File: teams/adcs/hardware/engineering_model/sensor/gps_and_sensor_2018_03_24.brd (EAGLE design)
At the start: 94 x 94 mm, 50 parts, among them U1 LT1761-X, U2 LT1761-X, U3 OEM719, U4 LTC3624

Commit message: ADCS/Sensor: Use picolock with more connectors and reformat component values
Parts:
- C1, C18, C2, C20, C22, C9: value 1u -> 1uF
- C10: value 22p -> 22pF
- C11, C17, C19, C21: value 10u -> 10uF
- C12: value 47u -> 47uF
- C13: value 22u -> 22uF
- C14, C15: value 230u -> DNP
- C16: value 1 uF -> 1uF
- C3, C4: value 4.7u -> 4.7uF
- C5, C6: value 0.01u -> 0.01uF
- C7: value 2.2u -> 2.2uF
- C8, C_SLEW_1: value 0.1u -> 0.1uF
- R5: value (none) -> 330
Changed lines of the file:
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@@
 <element name="U3" library="DubSat1 Components" package="OEM719" value="OEM719" x="62.484" y="5.842" rot="R90"/>
 <element name="U1" library="DubSat1 Components" package="SOT-23-5" value="LT1761-X" x="86.995" y="80.9625" rot="R270"/>
-<element name="C5" library="DubSat1 Components" package="0805" value="0.01u" x="90.17" y="80.9625" rot="R270"/>
-<element name="C1" library="DubSat1 Components" package="0805" value="1u" x="85.4075" y="84.455" rot="R270"/>
-<element name="C3" library="DubSat1 Components" package="0805" value="4.7u" x="92.3925" y="80.9625" rot="R90"/>
+<element name="C5" library="DubSat1 Components" package="0805" value="0.01uF" x="90.17" y="80.9625" rot="R270"/>
+<element name="C1" library="DubSat1 Components" package="0805" value="1uF" x="85.4075" y="84.455" rot="R270"/>
+<element name="C3" library="DubSat1 Components" package="0805" value="4.7uF" x="92.3925" y="80.9625" rot="R90"/>
 <element name="U2" library="DubSat1 Components" package="SOT-23-5" value="LT1761-X" x="14.605" y="80.9625" rot="R90"/>
-<element name="C6" library="DubSat1 Components" package="0805" value="0.01u" x="11.1125" y="80.9625" rot="R90"/>
-<element name="C2" library="DubSat1 Components" package="0805" value="1u" x="16.1925" y="84.455" rot="R270"/>
-<element name="C4" library="DubSat1 Components" package="0805" value="4.7u" x="8.89" y="80.9625" rot="R270"/>
+<element name="C6" library="DubSat1 Components" package="0805" value="0.01uF" x="11.1125" y="80.9625" rot="R90"/>
+<element name="C2" library="DubSat1 Components" package="0805" value="1uF" x="16.1925" y="84.455" rot="R270"/>
+<element name="C4" library="DubSat1 Components" package="0805" value="4.7uF" x="8.89" y="80.9625" rot="R270"/>
 <element name="PHOTODIODE" library="DubSat1 Components" package="PICOLOCK_4" value="PICOLOCK_4" x="76.708" y="14.986" rot="R180"/>
 <element name="R1" library="DubSat1 Components" package="0805" value="2.2k" x="67.31" y="12.954" rot="R270"/>
 <element name="R2" library="DubSat1 Components" package="0805" value="2.2k" x="67.31" y="8.89" rot="R270"/>
 <element name="U4" library="DubSat1 Components" package="LTC3624" value="LTC3624" x="69.596" y="70.612" rot="R270"/>
-<element name="C7" library="DubSat1 Components" package="0805" value="2.2u" x="70.358" y="66.294" rot="R270"/>
+<element name="C7" library="DubSat1 Components" package="0805" value="2.2uF" x="70.358" y="66.294" rot="R270"/>
 <element name="L1" library="DubSat1 Components" package="COILCRAFT_XAL4020" value="COILCRAFT_XAL4020-222ME" x="71.882" y="74.93"/>
 <element name="R3" library="DubSat1 Components" package="0805" value="0" x="72.898" y="67.818" rot="R90"/>
 <element name="R4" library="DubSat1 Components" package="0805" value="DNP" x="68.072" y="66.294" rot="R90"/>
-<element name="C10" library="DubSat1 Components" package="0805" value="22p" x="73.914" y="64.516"/>
-<element name="C8" library="DubSat1 Components" package="0805" value="0.1u" x="76.2" y="69.977"/>
-<element name="C9" library="DubSat1 Components" package="0805" value="1u" x="76.2" y="71.755"/>
-<element name="C11" library="DubSat1 Components" package="0805" value="10u" x="76.2" y="68.199"/>
-<element name="C12" library="DubSat1 Components" package="1206" value="47u" x="76.581" y="75.819"/>
+<element name="C10" library="DubSat1 Components" package="0805" value="22pF" x="73.914" y="64.516"/>
+<element name="C8" library="DubSat1 Components" package="0805" value="0.1uF" x="76.2" y="69.977"/>
+<element name="C9" library="DubSat1 Components" package="0805" value="1uF" x="76.2" y="71.755"/>
+<element name="C11" library="DubSat1 Components" package="0805" value="10uF" x="76.2" y="68.199"/>
+<element name="C12" library="DubSat1 Components" package="1206" value="47uF" x="76.581" y="75.819"/>
 <element name="U$1" library="HuskySat-1 Logos" package="LOGO_MOLEX" value="LOGO_MOLEX" x="37.846" y="13.462" rot="MR0"/>
-<element name="C_SLEW_1" library="DubSat1 Components" package="0805" value="0.1u" x="71.12" y="55.88"/>
+<element name="C_SLEW_1" library="DubSat1 Components" package="0805" value="0.1uF" x="71.12" y="55.88"/>
 <element name="R_PULLUP1" library="DubSat1 Components" package="0805" value="100k" x="73.66" y="58.42" smashed="yes" rot="R270">
 <attribute name="NAME" x="74.617325" y="59.63869375" size="0.4064" layer="25" font="vector" rot="R270"/>
@@
 </element>
 <element name="U$3" library="DubSat1 Components" package="TSOP-6" value="SI3865DDV" x="71.12" y="58.42" rot="R270"/>
-<element name="C14" library="DubSat1 Components" package="PANASONIC_SVPG" value="230u" x="87.63" y="57.912" rot="R270"/>
-<element name="C15" library="DubSat1 Components" package="PANASONIC_SVPG" value="230u" x="81.28" y="61.976" rot="R90"/>
-<element name="C13" library="DubSat1 Components" package="1206" value="22u" x="76.581" y="73.66"/>
+<element name="C14" library="DubSat1 Components" package="PANASONIC_SVPG" value="DNP" x="87.63" y="57.912" rot="R270"/>
+<element name="C15" library="DubSat1 Components" package="PANASONIC_SVPG" value="DNP" x="81.28" y="61.976" rot="R90"/>
+<element name="C13" library="DubSat1 Components" package="1206" value="22uF" x="76.581" y="73.66"/>
 <element name="U$2" library="DubSat1 Components" package="1X08_CONNECTOR" value="PROGRAM/DEBUG_PORT" x="93.218" y="15.748" rot="R90"/>
 <element name="D1" library="DubSat1 Components" package="LED-1206" value="" x="88.392" y="36.83" rot="R90"/>
-<element name="R5" library="DubSat1 Components" package="0805" value="" x="90.424" y="37.846" rot="R90"/>
+<element name="R5" library="DubSat1 Components" package="0805" value="330" x="90.424" y="37.846" rot="R90"/>
 <element name="J1" library="SparkFun-Connectors" package="1X06_LOCK" value="" x="64.516" y="63.754" rot="R90"/>
 <element name="J2" library="SparkFun-Connectors" package="1X03_LOCK" value="" x="64.262" y="12.446" rot="R270"/>
@@
 <attribute name="PROD_ID" value="CONN-09701" x="84.582" y="7.874" size="1.778" layer="27" rot="R90" display="off"/>
 </element>
-<element name="C16" library="DubSat1 Components" package="0805" value="1 uF" x="75.946" y="50.038"/>
-<element name="C17" library="DubSat1 Components" package="0805" value="10u" x="67.691" y="74.295" rot="R180"/>
-<element name="C18" library="DubSat1 Components" package="0805" value="1u" x="69.85" y="77.978"/>
-<element name="C19" library="DubSat1 Components" package="0805" value="10u" x="73.66" y="55.118" rot="R270"/>
-<element name="C20" library="DubSat1 Components" package="0805" value="1u" x="75.438" y="55.118" rot="R270"/>
-<element name="C21" library="DubSat1 Components" package="0805" value="10u" x="67.564" y="60.452" rot="R90"/>
-<element name="C22" library="DubSat1 Components" package="0805" value="1u" x="71.12" y="53.34" rot="R315"/>
+<element name="C16" library="DubSat1 Components" package="0805" value="1uF" x="75.946" y="50.038"/>
+<element name="C17" library="DubSat1 Components" package="0805" value="10uF" x="67.691" y="74.295" rot="R180"/>
+<element name="C18" library="DubSat1 Components" package="0805" value="1uF" x="69.85" y="77.978"/>
+<element name="C19" library="DubSat1 Components" package="0805" value="10uF" x="73.66" y="55.118" rot="R270"/>
+<element name="C20" library="DubSat1 Components" package="0805" value="1uF" x="75.438" y="55.118" rot="R270"/>
+<element name="C21" library="DubSat1 Components" package="0805" value="10uF" x="67.564" y="60.452" rot="R90"/>
+<element name="C22" library="DubSat1 Components" package="0805" value="1uF" x="71.12" y="53.34" rot="R315"/>
 <element name="R_PULLDOWN" library="DubSat1 Components" package="0805" value="100k" x="78.486" y="54.356" rot="R90"/>
 <element name="R6" library="DubSat1 Components" package="0805" value="100k" x="61.214" y="23.622" rot="R90"/>

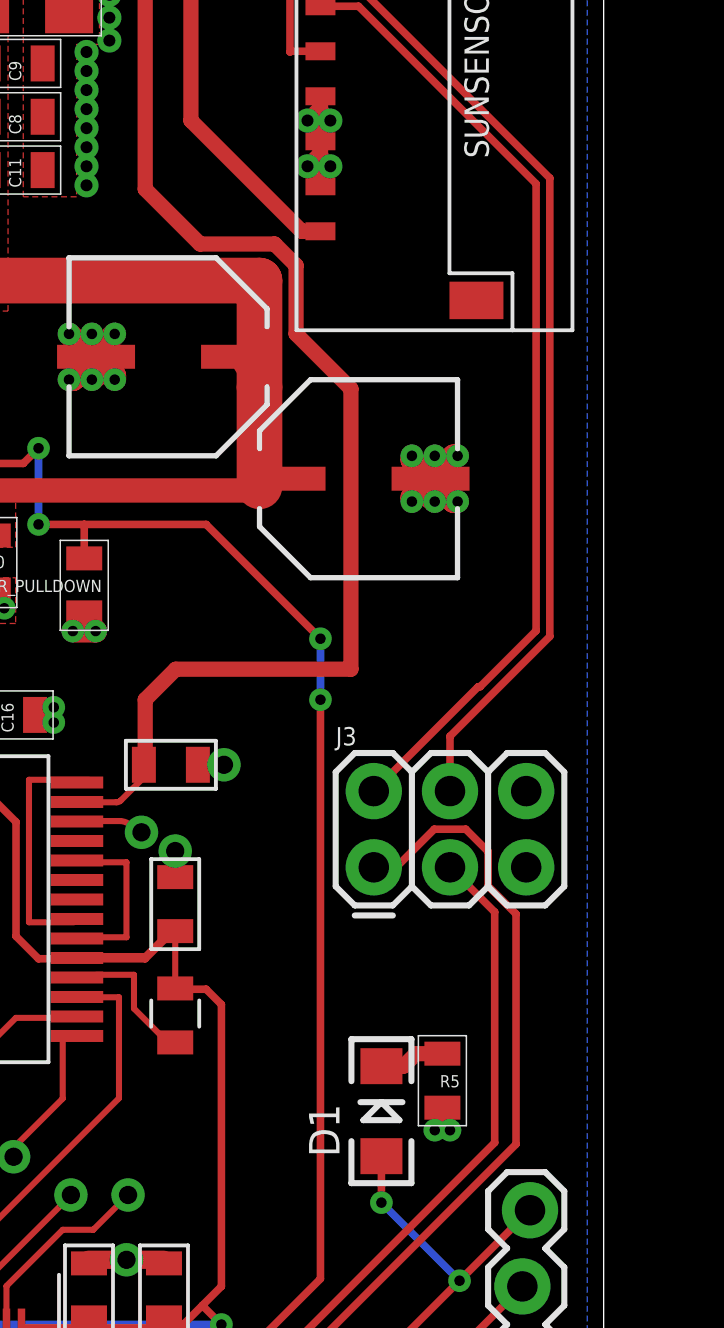
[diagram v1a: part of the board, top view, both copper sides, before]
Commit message: ADCS/Sensor: Added pin documentation
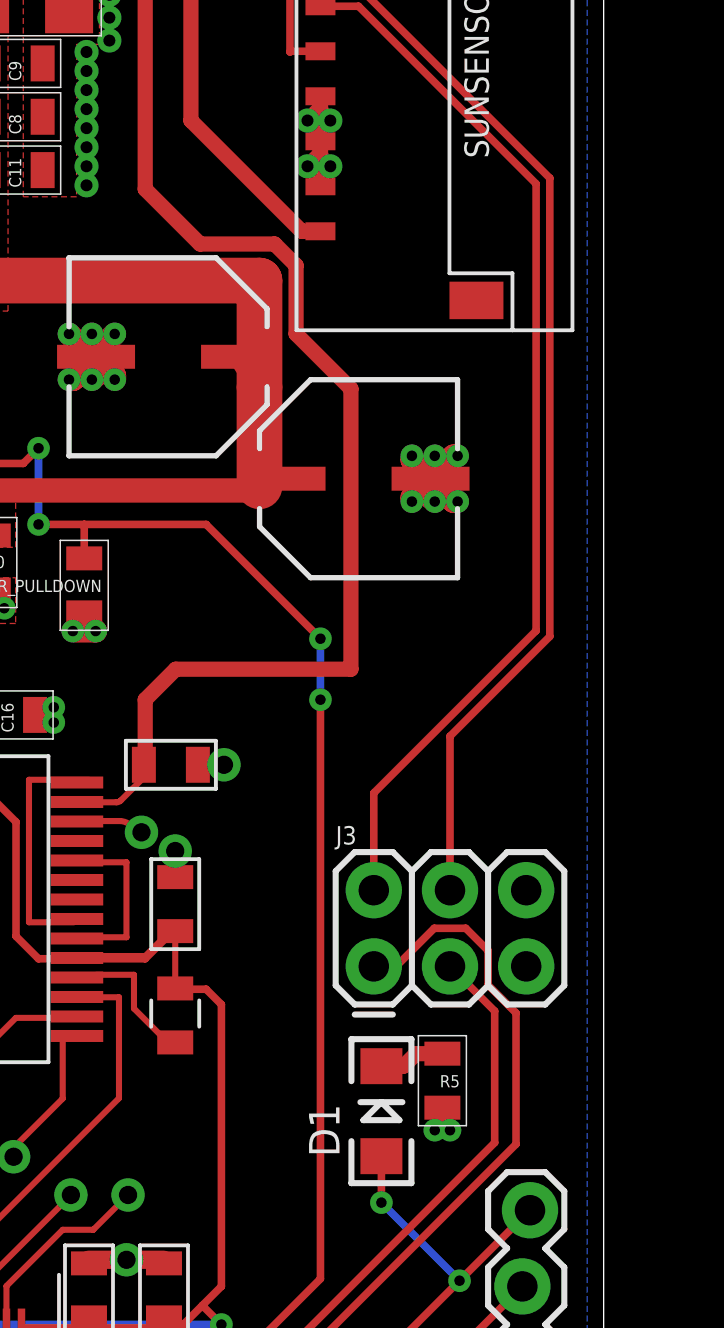
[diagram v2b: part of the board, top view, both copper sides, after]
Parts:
- moved J3 3.30 mm to (88.1, 41.7)
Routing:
- net I2C_SDA: track 82.7 -> 79.4 mm
- net SUNSENSOR_SCL: track 36.8 -> 40.1 mm
- net I2C_SCL: track 87.0 -> 83.7 mm
- net SUNSENSOR_SDA: track 32.2 -> 35.4 mm
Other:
- board text added: "BDOT GND"
- board text added: "GND"
- board text added: "P3.4 GPIO"
- board text added: "P3.5 GPIO"
- board text added: "PD_SCL"
- board text added: "PD_SDA"
- board text added: "RXD"
- board text added: "SBWTCK"
- board text added: "SBWTDIO"
- board text added: "SCL"
- board text added: "SDA"
- board text added: "SS_SCL"
- board text added: "SS_SDA"
- board text added: "TXD"
- board text added: "VBAT"
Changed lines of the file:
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@@
 <board>
 <plain>
+<wire x1="66.04" y1="90.17" x2="66.04" y2="85.09" width="0.1524" layer="49"/>
+<wire x1="66.04" y1="85.09" x2="66.04" y2="80.264" width="0.1524" layer="49"/>
+<wire x1="66.04" y1="80.264" x2="68.58" y2="80.264" width="0.1524" layer="49"/>
+<wire x1="68.58" y1="80.264" x2="68.58" y2="85.09" width="0.1524" layer="49"/>
+<wire x1="68.58" y1="85.09" x2="68.58" y2="90.17" width="0.1524" layer="49"/>
+<wire x1="68.58" y1="90.17" x2="66.04" y2="90.17" width="0.1524" layer="49"/>
+<wire x1="66.04" y1="85.09" x2="68.58" y2="85.09" width="0.1524" layer="49"/>
+<text x="68.072" y="90.678" size="1.778" layer="49" font="vector" rot="R90">GND</text>
+<text x="66.548" y="79.502" size="1.778" layer="49" font="vector" rot="R270">VBAT</text>
+<text x="88.138" y="46.736" size="1.27" layer="51" font="vector" rot="R90" align="center-left">SS_SDA</text>
+<text x="90.678" y="46.736" size="1.27" layer="51" font="vector" rot="R90" align="center-left">SS_SCL</text>
+<text x="93.218" y="46.736" size="1.27" layer="51" font="vector" rot="R90" align="center-left">GND</text>
+<text x="62.484" y="9.906" size="1.27" layer="51" font="vector" rot="R180" align="center-left">SDA</text>
+<text x="62.484" y="7.366" size="1.27" layer="51" font="vector" rot="R180" align="center-left">SCL</text>
+<text x="62.484" y="12.446" size="1.27" layer="51" font="vector" rot="R180" align="center-left">GND</text>
+<wire x1="80.772" y1="14.224" x2="80.772" y2="11.684" width="0.254" layer="49"/>
+<wire x1="80.772" y1="11.684" x2="80.772" y2="9.144" width="0.254" layer="49"/>
+<wire x1="80.772" y1="9.144" x2="80.772" y2="6.604" width="0.254" layer="49"/>
+<wire x1="80.772" y1="6.604" x2="83.312" y2="6.604" width="0.254" layer="49"/>
+<wire x1="83.312" y1="6.604" x2="83.312" y2="9.144" width="0.254" layer="49"/>
+<wire x1="83.312" y1="9.144" x2="83.312" y2="11.684" width="0.254" layer="49"/>
+<wire x1="83.312" y1="11.684" x2="83.312" y2="14.224" width="0.254" layer="49"/>
+<wire x1="83.312" y1="14.224" x2="80.772" y2="14.224" width="0.254" layer="49"/>
+<wire x1="80.772" y1="11.684" x2="83.312" y2="11.684" width="0.254" layer="49"/>
+<wire x1="80.772" y1="9.144" x2="83.312" y2="9.144" width="0.254" layer="49"/>
+<wire x1="83.312" y1="14.224" x2="85.852" y2="14.224" width="0.254" layer="49"/>
+<wire x1="85.852" y1="14.224" x2="85.852" y2="11.684" width="0.254" layer="49"/>
+<wire x1="85.852" y1="11.684" x2="85.852" y2="9.144" width="0.254" layer="49"/>
+<wire x1="85.852" y1="9.144" x2="85.852" y2="6.604" width="0.254" layer="49"/>
+<wire x1="85.852" y1="6.604" x2="83.312" y2="6.604" width="0.254" layer="49"/>
+<wire x1="85.852" y1="9.144" x2="83.312" y2="9.144" width="0.254" layer="49"/>
+<wire x1="85.852" y1="11.684" x2="83.312" y2="11.684" width="0.254" layer="49"/>
+<text x="86.614" y="12.954" size="1.778" layer="49" font="vector" align="center-left">GND</text>
+<text x="86.614" y="10.414" size="1.778" layer="49" font="vector" align="center-left">SCL</text>
+<text x="86.614" y="7.874" size="1.778" layer="49" font="vector" align="center-left">SDA</text>
+<text x="80.01" y="7.874" size="1.778" layer="49" font="vector" rot="R180" align="center-left">PD_SDA</text>
+<text x="80.01" y="10.414" size="1.778" layer="49" font="vector" rot="R180" align="center-left">PD_SCL</text>
+<text x="80.01" y="12.954" size="1.778" layer="49" font="vector" rot="R180" align="center-left">GND</text>
+<text x="98.806" y="28.448" size="1.778" layer="49" font="vector" align="center-left">BDOT GND</text>
+<text x="98.806" y="25.908" size="1.778" layer="49" font="vector" align="center-left">BDOT GND</text>
+<text x="98.806" y="15.748" size="1.778" layer="49" font="vector" align="center-left">SBWTCK</text>
+<text x="98.806" y="18.288" size="1.778" layer="49" font="vector" align="center-left">SBWTDIO</text>
+<text x="98.806" y="20.828" size="1.778" layer="49" font="vector" align="center-left">TXD</text>
+<text x="98.806" y="23.368" size="1.778" layer="49" font="vector" align="center-left">RXD</text>
+<text x="98.806" y="30.988" size="1.778" layer="49" font="vector" align="center-left">P3.4 GPIO</text>
+<text x="98.806" y="33.528" size="1.778" layer="49" font="vector" align="center-left">P3.5 GPIO</text>
 </plain>
 <attributes>
@@
 <element name="J1" library="SparkFun-Connectors" package="1X06_LOCK" value="" x="64.516" y="63.754" rot="R90"/>
 <element name="J2" library="SparkFun-Connectors" package="1X03_LOCK" value="" x="64.262" y="12.446" rot="R270"/>
-<element name="J3" library="SparkFun-Connectors" package="2X3" value="" x="88.138" y="44.958">
-<attribute name="PROD_ID" value="CONN-09701" x="88.138" y="44.958" size="1.778" layer="27" display="off"/>
+<element name="J3" library="SparkFun-Connectors" package="2X3" value="" x="88.138" y="41.656">
+<attribute name="PROD_ID" value="CONN-09701" x="88.138" y="41.656" size="1.778" layer="27" display="off"/>
 </element>
 <element name="J4" library="SparkFun-Connectors" package="2X3" value="" x="84.582" y="7.874" rot="R90">
@@
 <wire x1="83.82" y1="6.096" x2="84.582" y2="6.858" width="0.254" layer="1"/>
 <wire x1="84.582" y1="6.858" x2="84.582" y2="7.874" width="0.254" layer="1"/>
-<wire x1="91.948" y1="45.48405625" x2="91.20405625" y2="46.228" width="0.254" layer="1"/>
-<wire x1="91.20405625" y1="46.228" x2="90.15194375" y2="46.228" width="0.254" layer="1"/>
-<wire x1="91.948" y1="44.33458125" x2="91.948" y2="45.48405625" width="0.254" layer="1"/>
-<wire x1="92.879" y1="35.729" x2="92.879" y2="43.40358125" width="0.254" layer="1"/>
-<wire x1="92.879" y1="43.40358125" x2="91.948" y2="44.33458125" width="0.254" layer="1"/>
-<wire x1="88.88194375" y1="44.958" x2="88.138" y2="44.958" width="0.254" layer="1"/>
-<wire x1="90.15194375" y1="46.228" x2="88.88194375" y2="44.958" width="0.254" layer="1"/>
+<wire x1="91.948" y1="42.18205625" x2="91.20405625" y2="42.926" width="0.254" layer="1"/>
+<wire x1="91.20405625" y1="42.926" x2="90.15194375" y2="42.926" width="0.254" layer="1"/>
+<wire x1="91.948" y1="41.03258125" x2="91.948" y2="42.18205625" width="0.254" layer="1"/>
+<wire x1="92.879" y1="35.729" x2="92.879" y2="40.10158125" width="0.254" layer="1"/>
+<wire x1="92.879" y1="40.10158125" x2="91.948" y2="41.03258125" width="0.254" layer="1"/>
+<wire x1="88.88194375" y1="41.656" x2="88.138" y2="41.656" width="0.254" layer="1"/>
+<wire x1="90.15194375" y1="42.926" x2="88.88194375" y2="41.656" width="0.254" layer="1"/>
 <wire x1="64.135" y1="9.906" x2="65.212" y2="9.906" width="0.254" layer="1"/>
 <wire x1="65.212" y1="9.906" x2="67.31" y2="12.054" width="0.254" layer="1"/>
@@
 <wire x1="83.312" y1="9.144" x2="84.582" y2="10.414" width="0.254" layer="1"/>
 <wire x1="83.312" y1="7.34794375" x2="83.312" y2="9.144" width="0.254" layer="1"/>
-<wire x1="92.1678" y1="35.7798" x2="92.1678" y2="43.4682" width="0.254" layer="1"/>
-<wire x1="92.1678" y1="43.4682" x2="90.678" y2="44.958" width="0.254" layer="1"/>
+<wire x1="92.1678" y1="35.7798" x2="92.1678" y2="40.1662" width="0.254" layer="1"/>
+<wire x1="92.1678" y1="40.1662" x2="90.678" y2="41.656" width="0.254" layer="1"/>
 <wire x1="64.389" y1="7.366" x2="65.024" y2="7.366" width="0.254" layer="1"/>
 <wire x1="65.024" y1="7.366" x2="65.8368" y2="6.5532" width="0.254" layer="1"/>
@@
 <signal name="SUNSENSOR_SCL">
 <contactref element="J3" pad="4"/>
-<wire x1="90.678" y1="47.498" x2="90.678" y2="49.32723125" width="0.254" layer="1"/>
-<wire x1="90.678" y1="49.32723125" x2="94.0054" y2="52.65463125" width="0.254" layer="1"/>
 <contactref element="SUNSENSOR" pad="P$2"/>
 <wire x1="94.0054" y1="67.93118125" x2="87.26058125" y2="74.676" width="0.254" layer="1"/>
@@
 <wire x1="85.368" y1="72.16" x2="86.36" y2="72.16" width="0.254" layer="1"/>
 <wire x1="94.0054" y1="52.65463125" x2="94.0054" y2="67.93118125" width="0.254" layer="1"/>
+<wire x1="90.678" y1="44.196" x2="90.678" y2="49.32723125" width="0.254" layer="1"/>
+<wire x1="90.678" y1="49.32723125" x2="94.0054" y2="52.65463125" width="0.254" layer="1"/>
 </signal>
 <signal name="SUNSENSOR_SDA">
 <contactref element="J3" pad="2"/>
-<wire x1="91.6819875" y1="50.9778" x2="93.5482" y2="52.8440125" width="0.254" layer="1"/>
-<wire x1="88.138" y1="47.498" x2="91.6178" y2="50.9778" width="0.254" layer="1"/>
-<wire x1="91.6178" y1="50.9778" x2="91.6819875" y2="50.9778" width="0.254" layer="1"/>
 <contactref element="SUNSENSOR" pad="P$1"/>
 <wire x1="93.5482" y1="67.7418" x2="87.63" y2="73.66" width="0.254" layer="1"/>
 <wire x1="87.63" y1="73.66" x2="86.36" y2="73.66" width="0.254" layer="1"/>
-<wire x1="93.5482" y1="52.8440125" x2="93.5482" y2="67.7418" width="0.254" layer="1"/>
+<wire x1="93.5482" y1="67.7418" x2="93.5482" y2="52.8440125" width="0.254" layer="1"/>
+<wire x1="88.138" y1="47.4338125" x2="88.138" y2="44.196" width="0.254" layer="1"/>
+<wire x1="93.5482" y1="52.8440125" x2="88.138" y2="47.4338125" width="0.254" layer="1"/>
 </signal>
 <signal name="PHOTODIODE_SCL">
